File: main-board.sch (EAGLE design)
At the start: 56 parts, among them IC1 MEGA328-PB, IC2 MCP73831, IC3 LE33, Q1 3,6864 MHz, Q4 TSM2302CX, T1 IRF7306

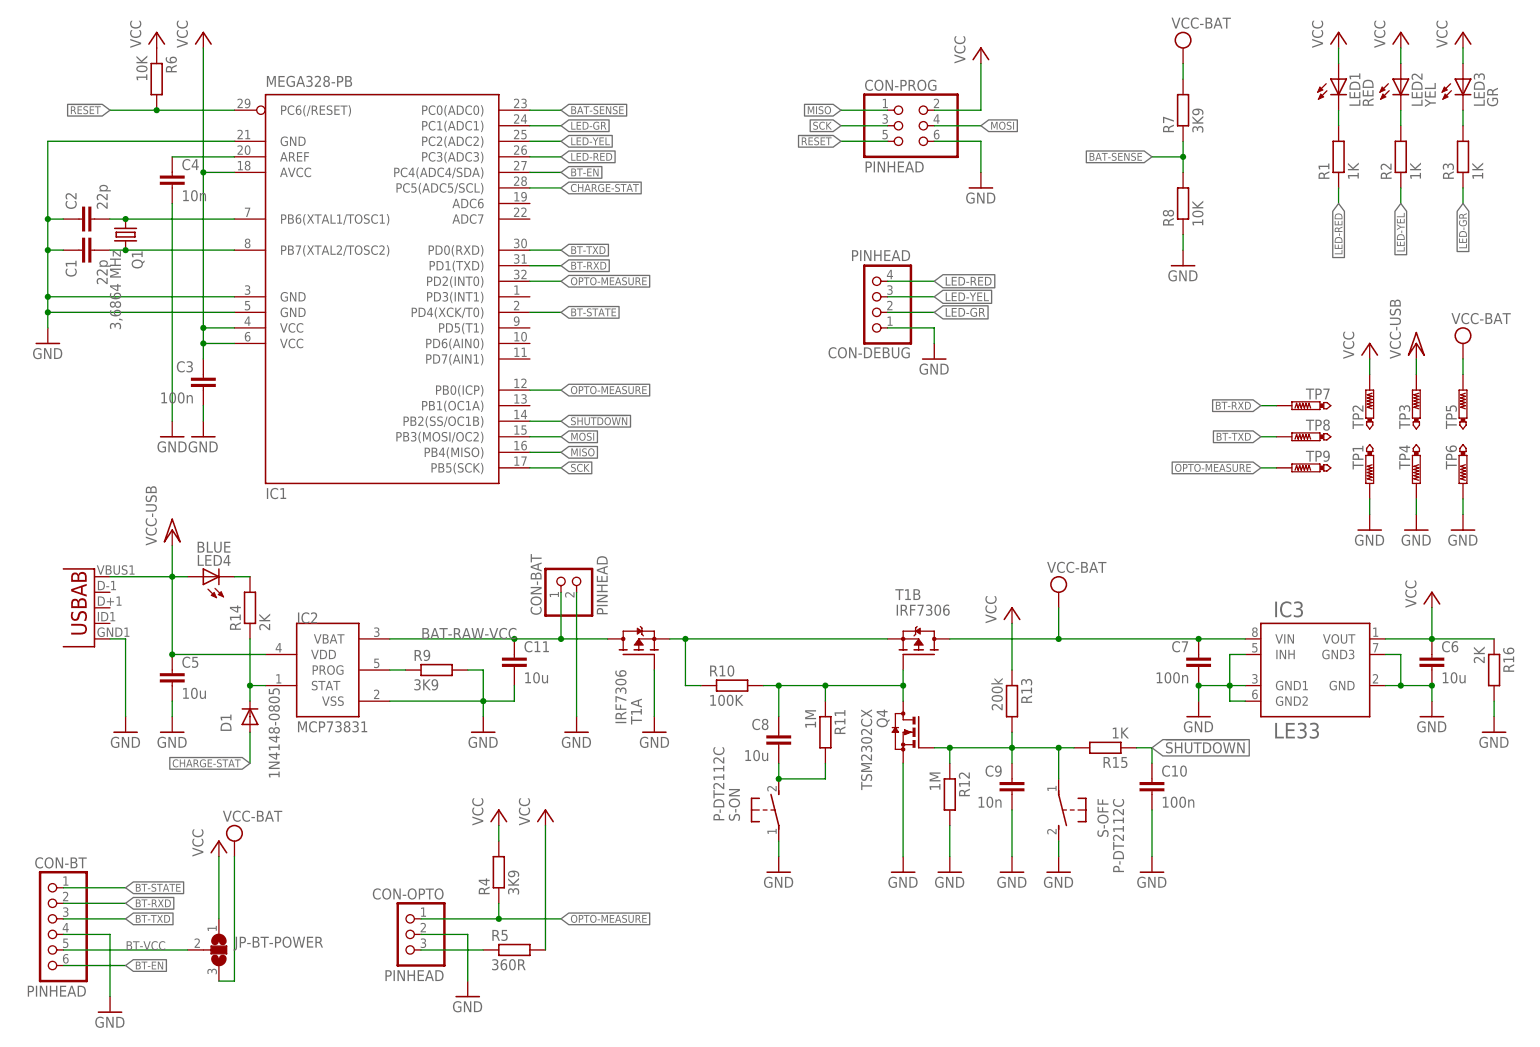
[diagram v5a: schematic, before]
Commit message: Set R4 to 100k.
The construction of second protoype showed that the value of the pull-up
is critical for proper device function.
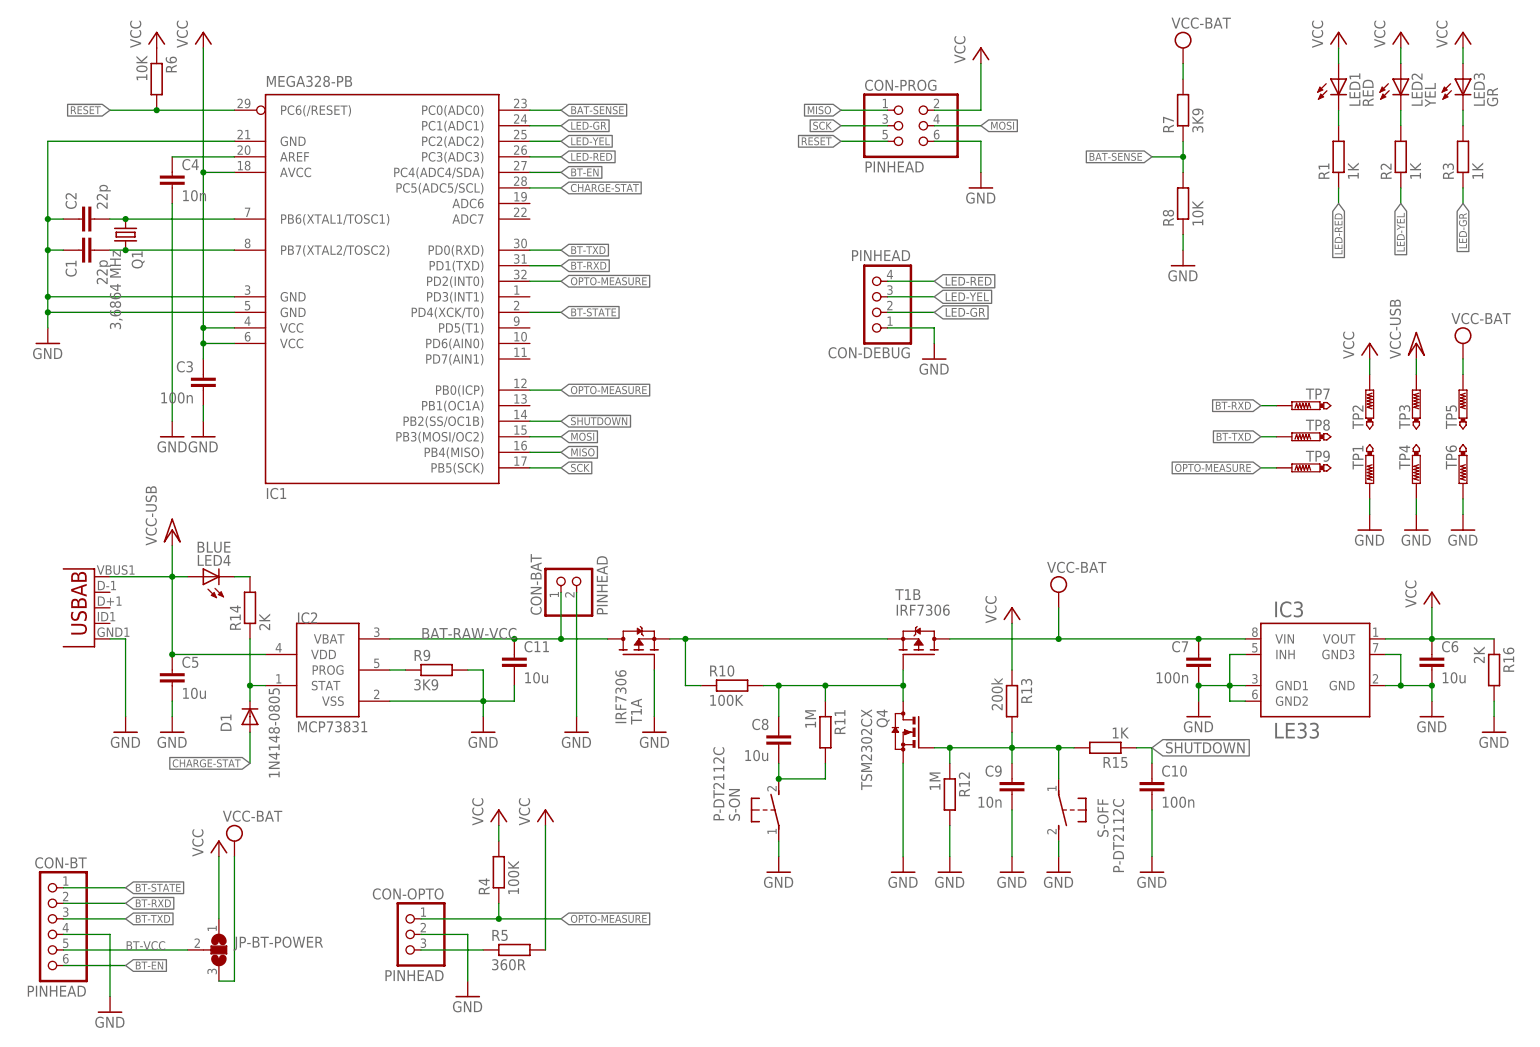
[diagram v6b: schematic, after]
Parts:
- R4: value 3K9 -> 100K
